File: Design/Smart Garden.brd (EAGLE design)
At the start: 86 x 79 mm, 88 parts, among them IC2 MP1584EN-LF-Z, J2 POWER_JACK, T1 MMBT2222A, T3 MMBT2222A, T5 MMBT2222A, T7 MMBT2222A, U1 ESP-32S, U3 LM2596S, U4 DB107S

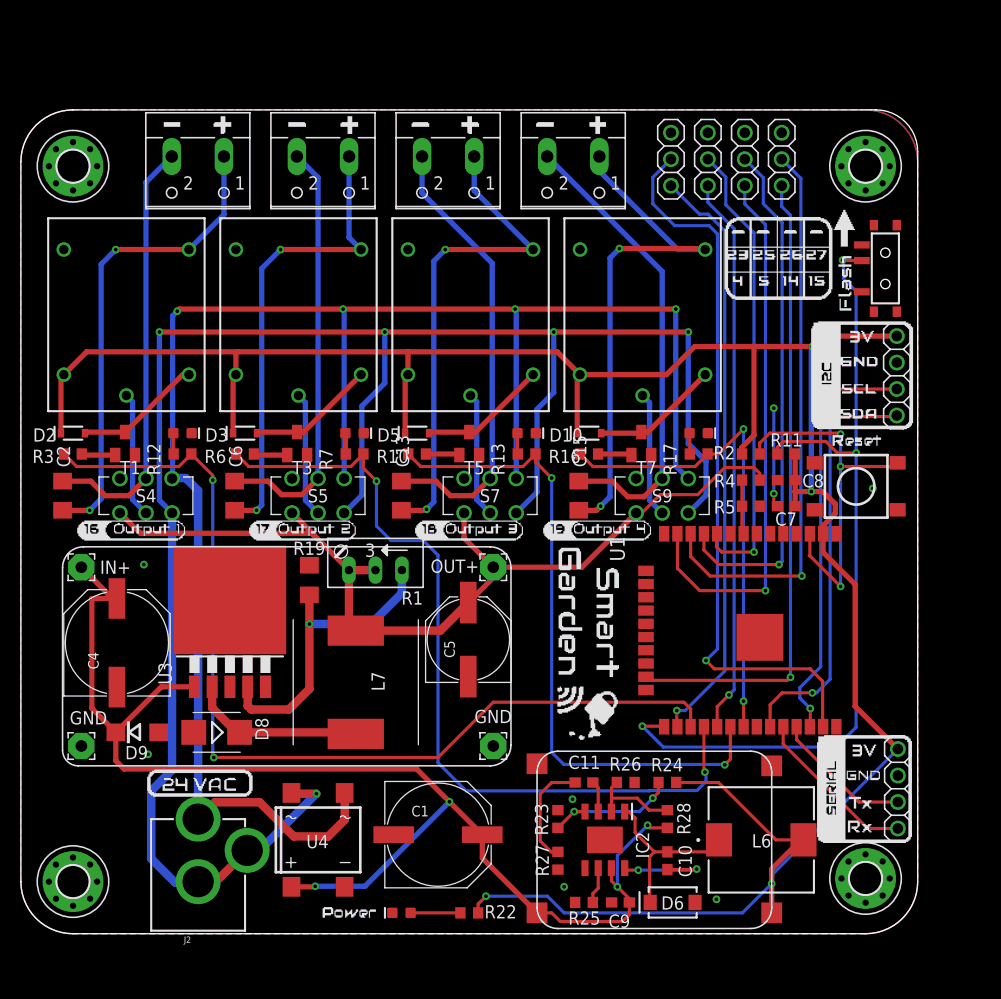
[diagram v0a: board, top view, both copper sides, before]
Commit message: First commit to the CP2102 branch with schematic and a first layout of the CP2102
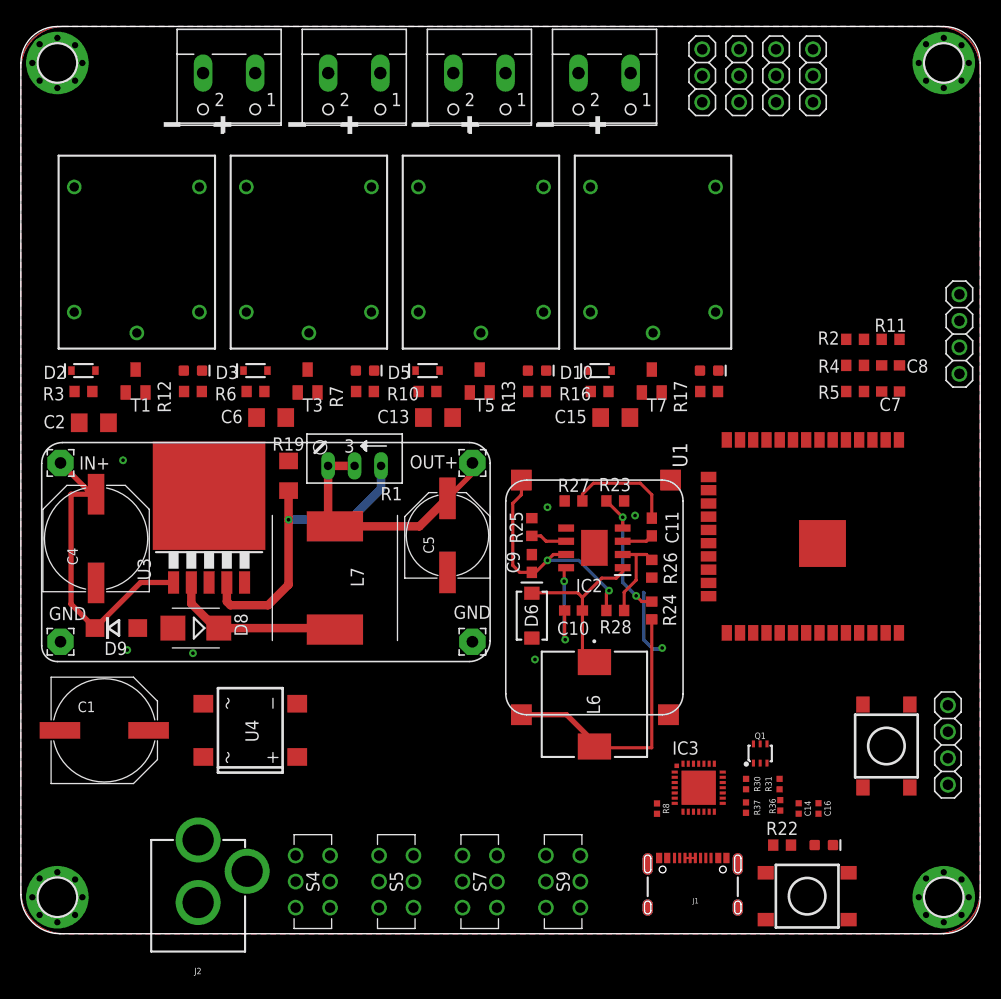
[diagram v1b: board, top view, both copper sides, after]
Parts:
- removed H2, H3, H4: MOUNT-PAD-ROUND, SpaceDIY_connectors:3,0-PAD
- added C14: 0.1uF, SparkFun-Capacitors:0402-TIGHT
- added C16: 4.7uF, SparkFun-Capacitors:0402-TIGHT
- added IC3: CP2102, silabs:MLP28
- added J1: USB-C, SparkFun-Connectors:USB-C-16P-4LAYER-ISOLATED
- added Q1: MBT3904DW1T1, SparkFun-DiscreteSemi:SC70-6
- added R30, R31, R8: 10k, SparkFun-Resistors:0402-TIGHT
- added R36, R37: 5.1k, SparkFun-Resistors:0402-TIGHT
- H1: value MOUNT-PAD-ROUND -> 92X84; device SpaceDIY_connectors:3,0-PAD -> SpaceDIY_symbols:92X87
- S1: value SWITCH_SPDT -> Reset; device SparkFun-Retired:KPS-1290 -> Testing:TACTILE_SWITCH_TALL
- moved S1 45.8 mm to (83.0, 18.0)
- moved TP1 41.5 mm to (48.0, 43.5), turned to 270 degrees
- moved LED2 41.0 mm to (77.0, 8.50), turned to 0 degrees
- moved S4 40.3 mm to (28.0, 5.00), turned to 90 degrees
- moved S2 39.6 mm to (75.4, 3.60), turned to 180 degrees
- moved S9 38.2 mm to (52.0, 5.00), turned to 90 degrees
- moved S5 37.8 mm to (36.0, 5.00), turned to 90 degrees
- moved S7 37.0 mm to (44.0, 5.00), turned to 90 degrees
- moved R25 36.3 mm to (49.0, 39.0), turned to 90 degrees
- moved R27 34.5 mm to (53.0, 41.5), turned to 180 degrees
- moved C9 33.6 mm to (49.0, 35.5), turned to 90 degrees
- moved C1 33.5 mm to (8.00, 19.5)
- moved R23 31.0 mm to (57.0, 41.5), turned to 0 degrees
- moved R22 30.7 mm to (73.0, 8.50), turned to 180 degrees
- moved D6 30.6 mm to (49.0, 30.5), turned to 90 degrees
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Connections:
- removed net RST: R2.1, S2.B2, U1.3
- new net CC3: J1.B5, R36.2
- new net CC4: J1.A5, R37.2
- new net D+: IC3.4, J1.A6, J1.B6
- new net D-: IC3.5, J1.A7, J1.B7
- new net DTR: IC3.28, Q1.1, R30.1
- new net ESP_RST: Q1.3, R2.1, S2.B2, U1.3
- new net N$21: Q1.5, R30.2
- new net N$22: Q1.2, R31.2
- new net N$4: IC3.9, R8.2
- new net N$5: IC3.7, IC3.8
- new net RTS: IC3.24, Q1.4, R31.1
- new net RX0: IC3.26
- new net TX0: IC3.25
- new net V_USB: J1.VBUS1, J1.VBUS2
- net 3.3V: now also C14.1, C16.1, IC3.6, R8.1
- net GND: now also C14.2, C16.2, H1.B3,1, H1.B3,2, H1.B3,3, H1.B3,6, IC3.3, IC3.EXP, IC3.M, J1.GND, J1.GND2, R36.1, R37.1, S1.A2; no longer H1.B3,0, H1.P$2, H1.P$3, H1.P$4, H1.P$5, H1.P$6, H1.P$7, H1.P$8, H1.P$9, H2.B3,0, H2.P$2, H2.P$3, H2.P$4, H2.P$5, H2.P$6, H2.P$7, H2.P$8, H2.P$9, H3.B3,0, H3.P$2, H3.P$3, H3.P$4, H3.P$5, H3.P$6, H3.P$7, H3.P$8, H3.P$9, H4.B3,0, H4.P$2, H4.P$3, H4.P$4, H4.P$5, H4.P$6, H4.P$7, H4.P$8, H4.P$9, S1.O
- net IO0: now also Q1.6, S1.B2; no longer S1.P
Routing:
- net 3.3V: track 243.3 -> 27.5 mm, vias 4 -> 0
- net 24V1: track 181.8 -> 0.00 mm, vias 5 -> 0
- net 24V2: track 167.2 -> 0.00 mm, vias 4 -> 0
- net IO16: track 93.1 -> 0.14 mm, vias 2 -> 1
- net IO0: track 80.3 -> 0.00 mm, vias 3 -> 0
- net IO17: track 80.1 -> 6.90 mm, vias 2 -> 1
- net IO23: track 70.4 -> 0.00 mm, vias 1 -> 0
- net 24V: track 124.4 -> 55.4 mm, vias 4 -> 2
- net VCC: track 89.4 -> 25.4 mm
- net IO18: track 63.4 -> 0.00 mm, vias 2 -> 0
- net IO15: track 61.6 -> 0.00 mm, vias 1 -> 0
- net IO4: track 56.9 -> 0.00 mm, vias 1 -> 0
- net IO27: track 54.5 -> 0.00 mm, vias 1 -> 0
- net IO5: track 53.6 -> 0.00 mm, vias 1 -> 0
- net IO14: track 52.3 -> 0.00 mm, vias 1 -> 0
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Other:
- board size 86 x 79 mm -> 92 x 87 mm

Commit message: First commit to the CP2102 branch
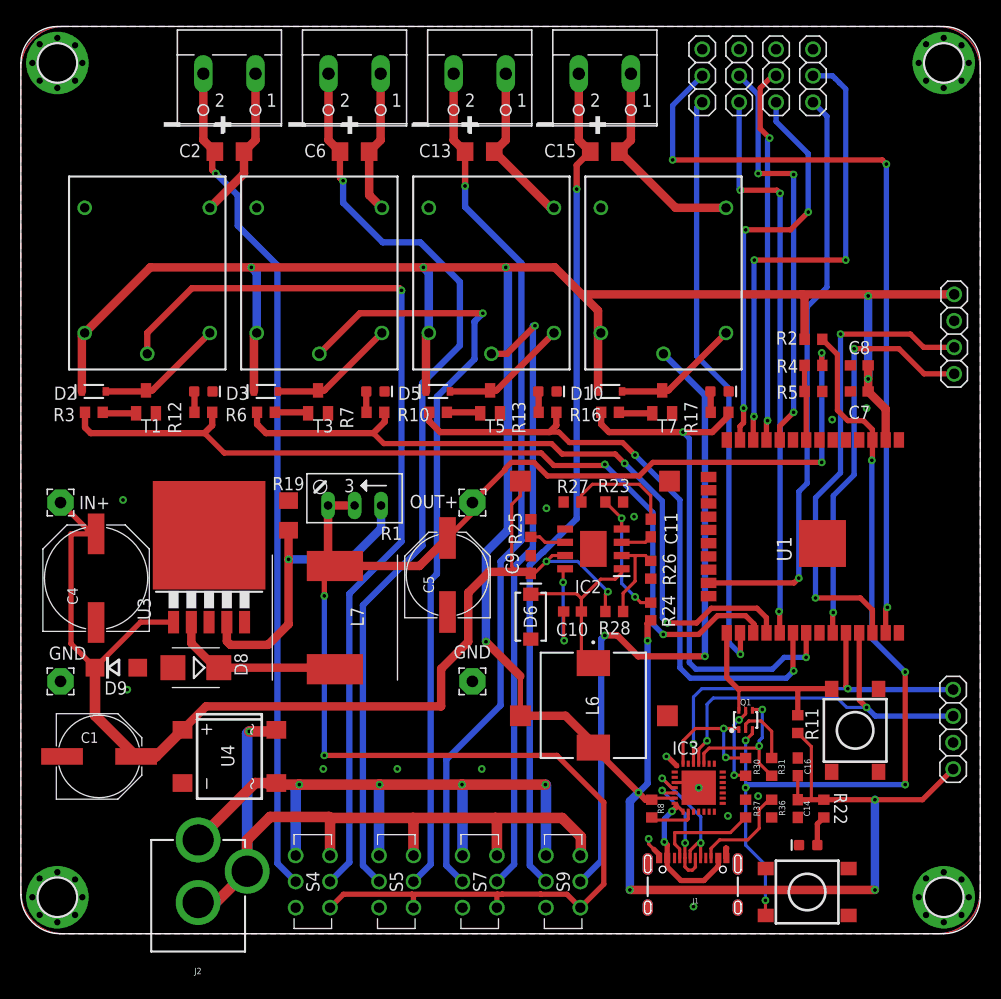
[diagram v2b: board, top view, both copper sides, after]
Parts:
- C1: value 330µ/50V -> 220µ/35V Low ESR; device rcl:PANASONIC_G -> rcl:PANASONIC_F
- C14, C16: device SparkFun-Capacitors:0402-TIGHT -> rcl:C0603
- R30, R31, R36, R37, R8: device SparkFun-Resistors:0402-TIGHT -> rcl:R0603
- moved R11 38.0 mm to (74.5, 20.1), turned to 90 degrees
- moved C2 29.1 mm to (20.0, 75.0)
- moved C6 26.7 mm to (32.0, 75.0)
- moved C13 25.8 mm to (44.0, 75.0)
- moved C15 25.5 mm to (56.0, 75.0)
- moved R22 5.32 mm to (77.0, 12.0), turned to 90 degrees
- moved C16 4.46 mm to (74.5, 16.0), turned to 90 degrees
- moved R2 4.00 mm to (76.0, 57.0)
- moved R4 4.00 mm to (76.0, 54.5)
- moved R5 4.00 mm to (76.0, 52.0)
- moved C4 3.80 mm to (7.21, 34.1)
- moved C5 3.80 mm to (40.9, 34.4)
- moved L7 3.80 mm to (30.1, 30.3)
- moved PAD1 3.80 mm to (3.80, 41.3)
- moved PAD3 3.80 mm to (43.3, 41.3)
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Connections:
- removed net N$5: IC3.7, IC3.8
- removed net RX0: IC3.26
- removed net TX0: IC3.25
- net GND: now also H1.P$1, H1.P$10, H1.P$11, H1.P$12, H1.P$13, H1.P$14, H1.P$15, H1.P$16, H1.P$17, H1.P$18, H1.P$19, H1.P$2, H1.P$20, H1.P$21, H1.P$22, H1.P$23, H1.P$24, H1.P$25, H1.P$26, H1.P$27, H1.P$28, H1.P$29, H1.P$3, H1.P$30, H1.P$31, H1.P$32, H1.P$4, H1.P$5, H1.P$6, H1.P$7, H1.P$8, H1.P$9
- net RX: now also IC3.26
- net TX: now also IC3.25
- net V_USB: now also IC3.7, IC3.8
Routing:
- net 3.3V: track 27.5 -> 299.1 mm, vias 0 -> 11
- net VCC: track 25.4 -> 159.4 mm, vias 0 -> 4
- net N$17: track 0.00 -> 89.3 mm, vias 0 -> 1
- net N$1: track 0.00 -> 87.8 mm, vias 0 -> 1
- net IO16: track 0.14 -> 84.4 mm, vias 1 -> 2
- net N$31: track 0.00 -> 83.8 mm, vias 0 -> 1
- net N$2: track 0.00 -> 81.5 mm, vias 0 -> 1
- net ESP_RST: track 0.00 -> 81.2 mm, vias 0 -> 6
- net N$51: track 0.00 -> 81.0 mm, vias 0 -> 1
- net IO23: track 0.00 -> 75.0 mm, vias 0 -> 3
- net N$16: track 0.00 -> 74.5 mm, vias 0 -> 1
- net 24V1: track 0.00 -> 71.5 mm, vias 0 -> 1
- net N$50: track 0.00 -> 65.7 mm, vias 0 -> 2
- net 24V2: track 0.00 -> 63.8 mm, vias 0 -> 4
- net IO17: track 6.90 -> 69.3 mm, vias 1 -> 2
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
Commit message: Updated design files
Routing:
- net V_USB: track 14.5 -> 15.4 mm, vias 2 -> 3
- net CC3: track 9.72 -> 10.3 mm
- net GND: track 8.15 -> 8.13 mm, vias 15 -> 18

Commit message: Updated design files
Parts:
- removed Q1: MBT3904DW1T1, SparkFun-DiscreteSemi:SC70-6
- added T2: MMBT3904, transistor-neu-to92:SOT23-BEC
- added T4: MMBT2222A, transistor:SOT23
- D8: value SS34 -> 3A/40V/500mV; device diode:SMB -> SparkFun-DiscreteSemi:SMA-DIODE
- D9: value RS1G -> US1M
- R23: value 40.2k -> 39k
- R24: value 124k -> 120k
- R26: value 24.9k -> 24k
- R27: value 68.1k -> 68k
- S1, S2: device Testing:TACTILE_SWITCH_TALL -> SpaceDIY_electromechanical:TACTILE_SWITCH_SMD_5.2MM
- T1: value MMBT2222A -> MMBT3904; device transistor:SOT23 -> transistor-neu-to92:SOT23-BEC
- moved T1 64.3 mm to (68.5, 20.4)
- moved T3 16.5 mm to (12.0, 51.0)
- moved X6 5.06 mm to (51.0, 82.0)
- moved C15 4.50 mm to (51.5, 75.0)
- moved X4 4.08 mm to (40.0, 82.0)
- moved C13 4.00 mm to (40.0, 75.0)
- moved JP5 3.35 mm to (62.0, 82.5)
- moved X2 3.10 mm to (29.0, 82.0)
- moved C6 3.00 mm to (29.0, 75.0)
- moved X7 2.15 mm to (18.0, 82.0)
- moved C2 2.00 mm to (18.0, 75.0)
- moved JP4 1.89 mm to (67.0, 82.5)
- moved JP2 1.07 mm to (77.0, 82.5)
- moved LED2 1.00 mm to (75.5, 7.50)
- moved JP3 0.48 mm to (72.0, 82.5)
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- renumbered T7 to T6
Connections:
- net DTR: now also T1.E; no longer Q1.1
- net ESP_RST: now also S2.3, T2.C; no longer Q1.3, S2.B2
- net GND: now also S1.1, S2.1, T4.2; no longer S1.A2, S2.A2, T1.2
- net IO0: now also S1.3, T1.C; no longer Q1.6, S1.B2
- net N$12: now also T4.3; no longer T3.3
- net N$13: now also T4.1; no longer T3.1
- net N$21: now also T2.B; no longer Q1.5
- net N$22: now also T1.B; no longer Q1.2
- net N$7: now also T3.3; no longer T1.3
- net N$9: now also T3.1; no longer T1.1
- net RTS: now also T2.E; no longer Q1.4
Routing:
- net N$52: track 20.4 -> 25.5 mm
- net N$32: track 15.9 -> 20.7 mm
- net ESP_RST: track 81.2 -> 76.6 mm, vias 6 -> 5
- net N$22: track 6.11 -> 8.91 mm
- net N$21: track 7.83 -> 5.21 mm, vias 2 -> 0
- net N$31: track 83.8 -> 86.2 mm
- net N$19: track 13.8 -> 15.9 mm
- net N$17: track 89.3 -> 91.3 mm
- net N$51: track 81.0 -> 82.8 mm
- net IO23: track 75.0 -> 76.7 mm, vias 3 -> 2
- net N$2: track 81.5 -> 83.1 mm
- net DTR: track 12.9 -> 11.4 mm, vias 2 -> 0
- net IO4: track 57.0 -> 58.1 mm
- net IO0: track 19.4 -> 20.4 mm
- net IO25: track 39.6 -> 40.6 mm
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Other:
- board text added: "JLCJLCJLCJLC"
